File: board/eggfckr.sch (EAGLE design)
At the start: 8 parts, among them U1 ATTINY85-20PU

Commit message: dual
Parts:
- removed GND, VCC: (no value), microbuilder:HEADER-1X1ROUND
- added BATT1: FKIT-COIN_CELLLIR2450-H, SparkFun-Electromechanical:FKIT-COIN_CELLLIR2450-H
- added JP1: (no value), SparkFun-Connectors:AUDIO-JACKSPECIAL_POGO_PINS
- added RV1: (no value), SparkFun-Electromechanical:POT-RV16AF-20
- added U2: ATTINY85-20PU, Atmel_By_element14_Batch_1-00:ATTINY85-20PU
- S1: value SWITCH-MOMENTARY-2-SMD-1101NE -> (none); device ATtami:SWITCH-MOMENTARY-2-SMD-1101NE -> adafruit:EG1218S
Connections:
- new net N$6: LED2.A, U2.3(PB4)
- new net N$8: BATT1.NEG, S1.S
- net GND: now also BATT1.POS, JP1.SLEEVE, LED2.C, RV1.E, U2.4(GND); no longer GND.1
- net N$1: now also R1.1, U1.(PB1)6; no longer R2.2, U1.(PB2)7
- net N$2: now also LED1.A; no longer R1.2
- net N$3: now also JP1.LEFT, R1.2; no longer LED1.A, R1.1
- net N$4: now also RV1.S, U1.(PB2)7, U2.(PB2)7; no longer S1.2, U1.1(PB5)
- net N$5: now also R2.1, U2.(PB1)6; no longer S1.1, U1.2(PB3)
- net N$7: now also JP1.RIGHT, R2.2; no longer LED2.C, R2.1
- net VCC: now also RV1.A, S1.P, U2.(VCC)8; no longer LED2.A, VCC.1
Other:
- moved on the sheet: LED1, LED2, U1

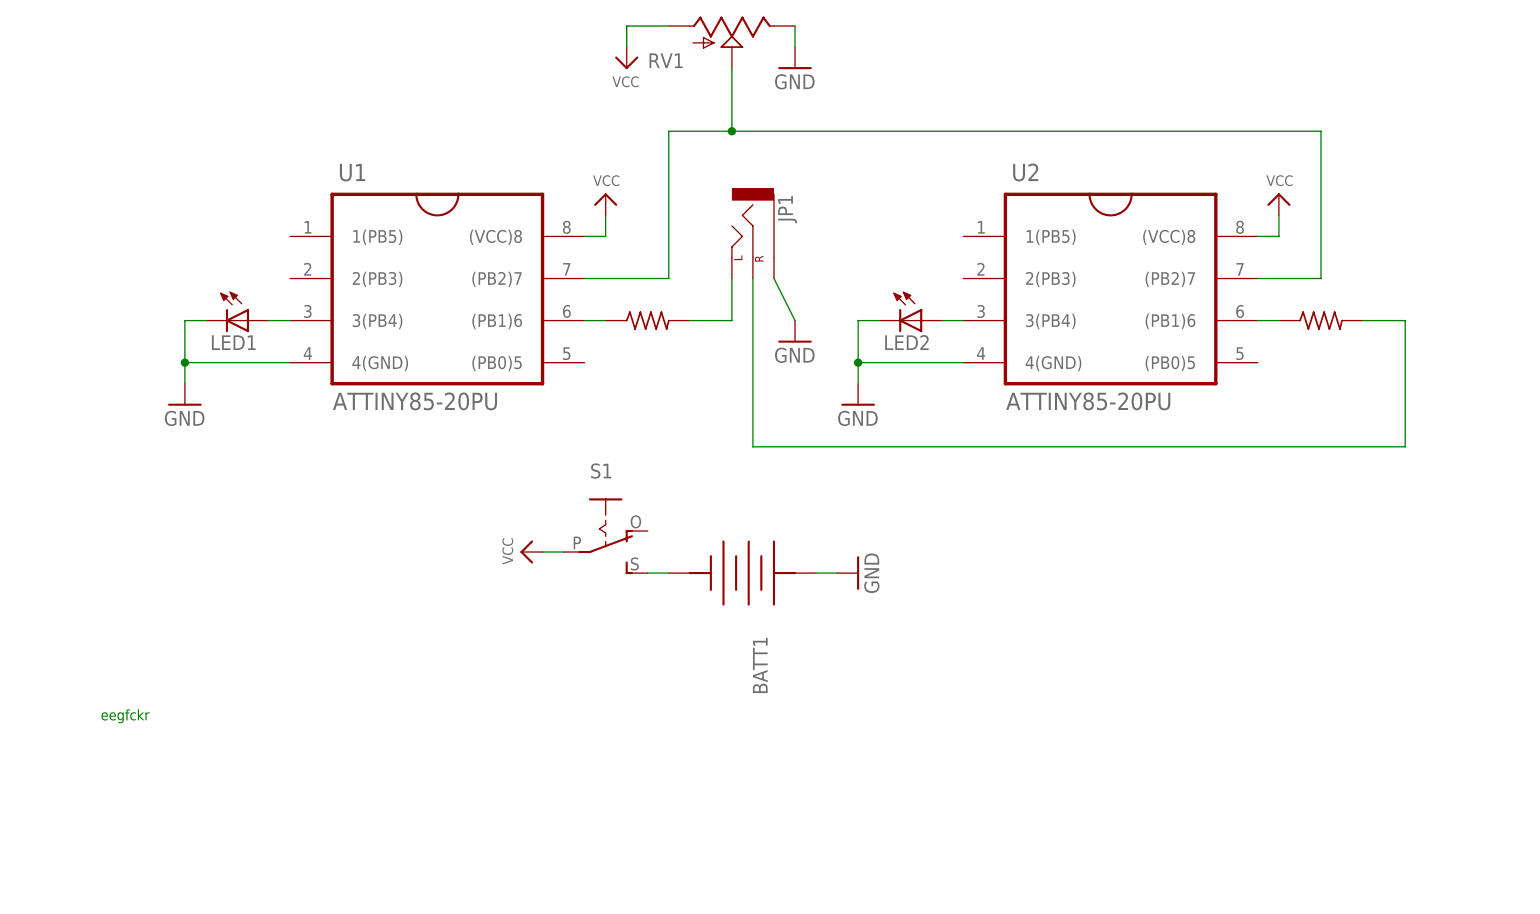
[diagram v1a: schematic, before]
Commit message: flipped attiny85
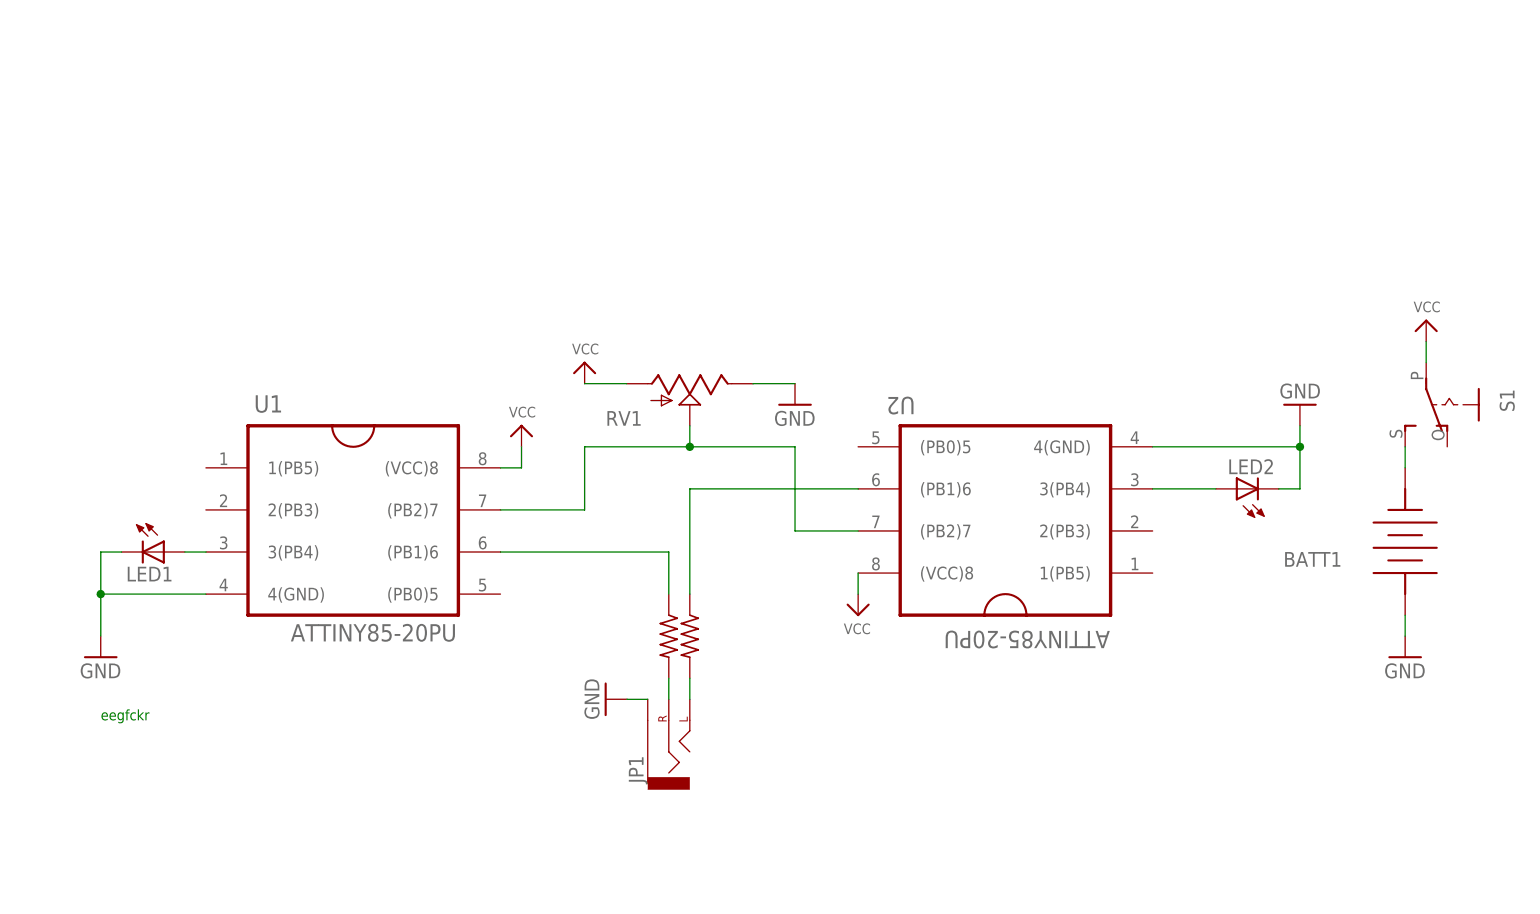
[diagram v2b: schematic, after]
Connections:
- net N$3: now also JP1.RIGHT; no longer JP1.LEFT
- net N$7: now also JP1.LEFT; no longer JP1.RIGHT
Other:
- moved on the sheet: BATT1, JP1, LED1, LED2, RV1, S1, U1, U2
